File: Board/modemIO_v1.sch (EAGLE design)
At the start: 24 parts, among them IC1 TLV320AIC14R-PDSO-G30, IC2 SN74LVC04ADRR-PDSO-G14, Q1-18.432MHZ ASFL1

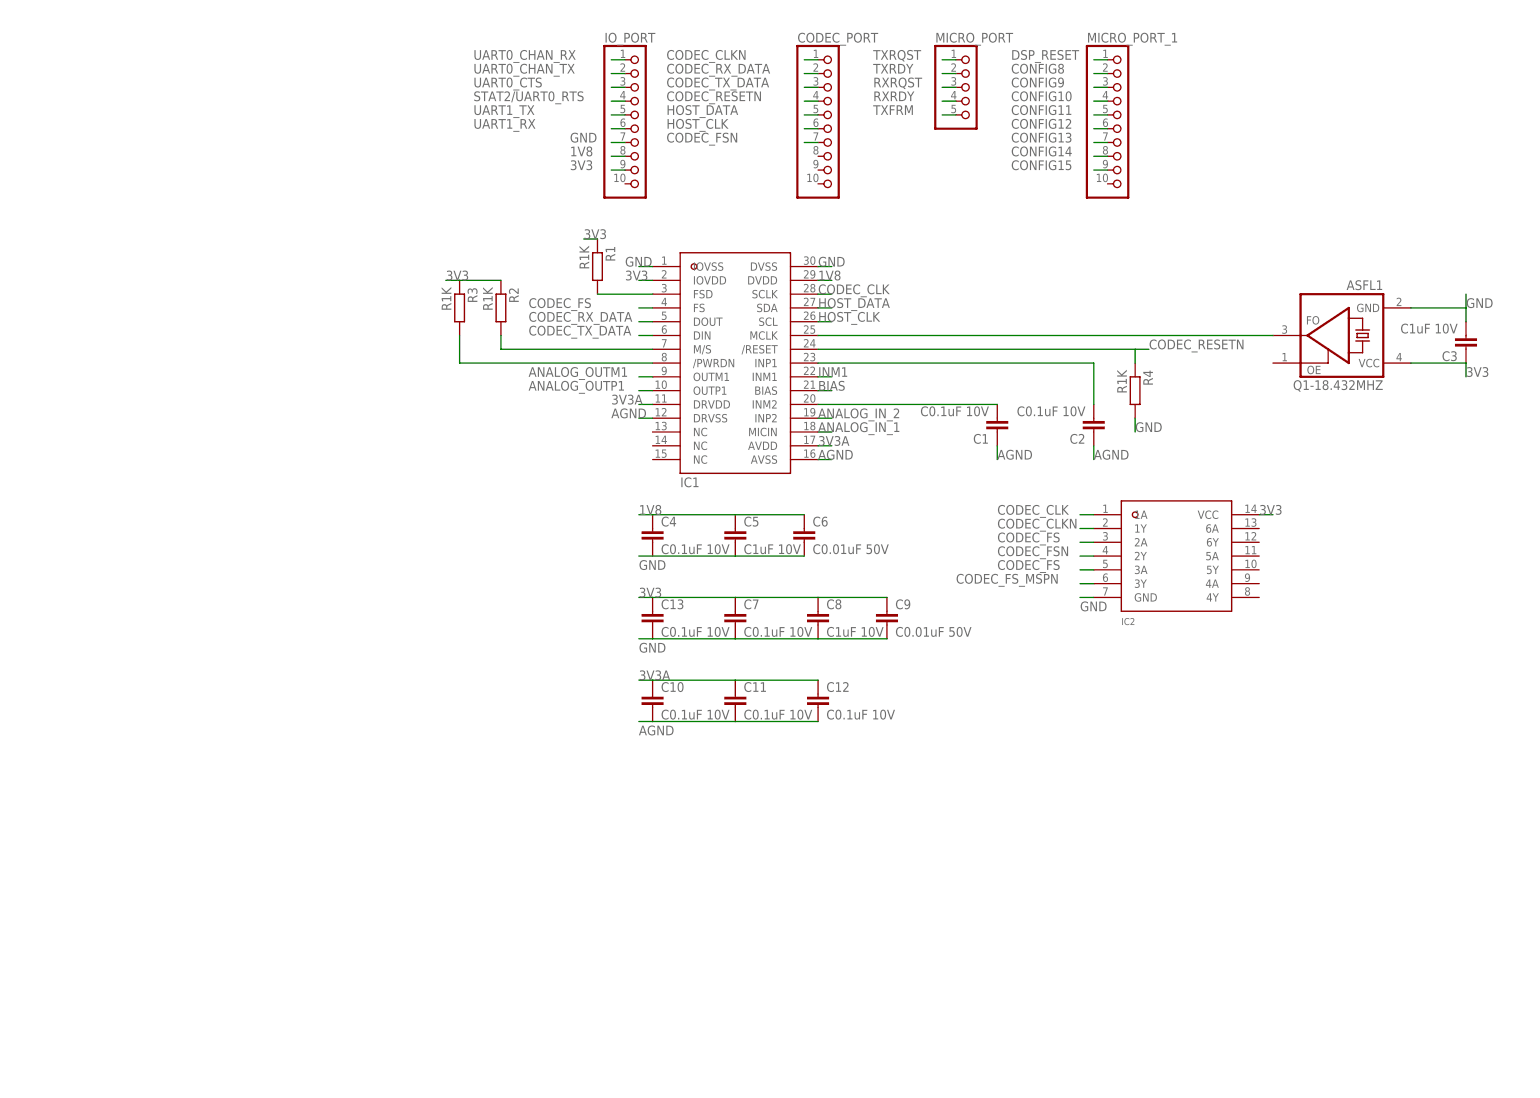
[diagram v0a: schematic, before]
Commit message: + pull up to AMBE's Reset & progress in ModemIO brd
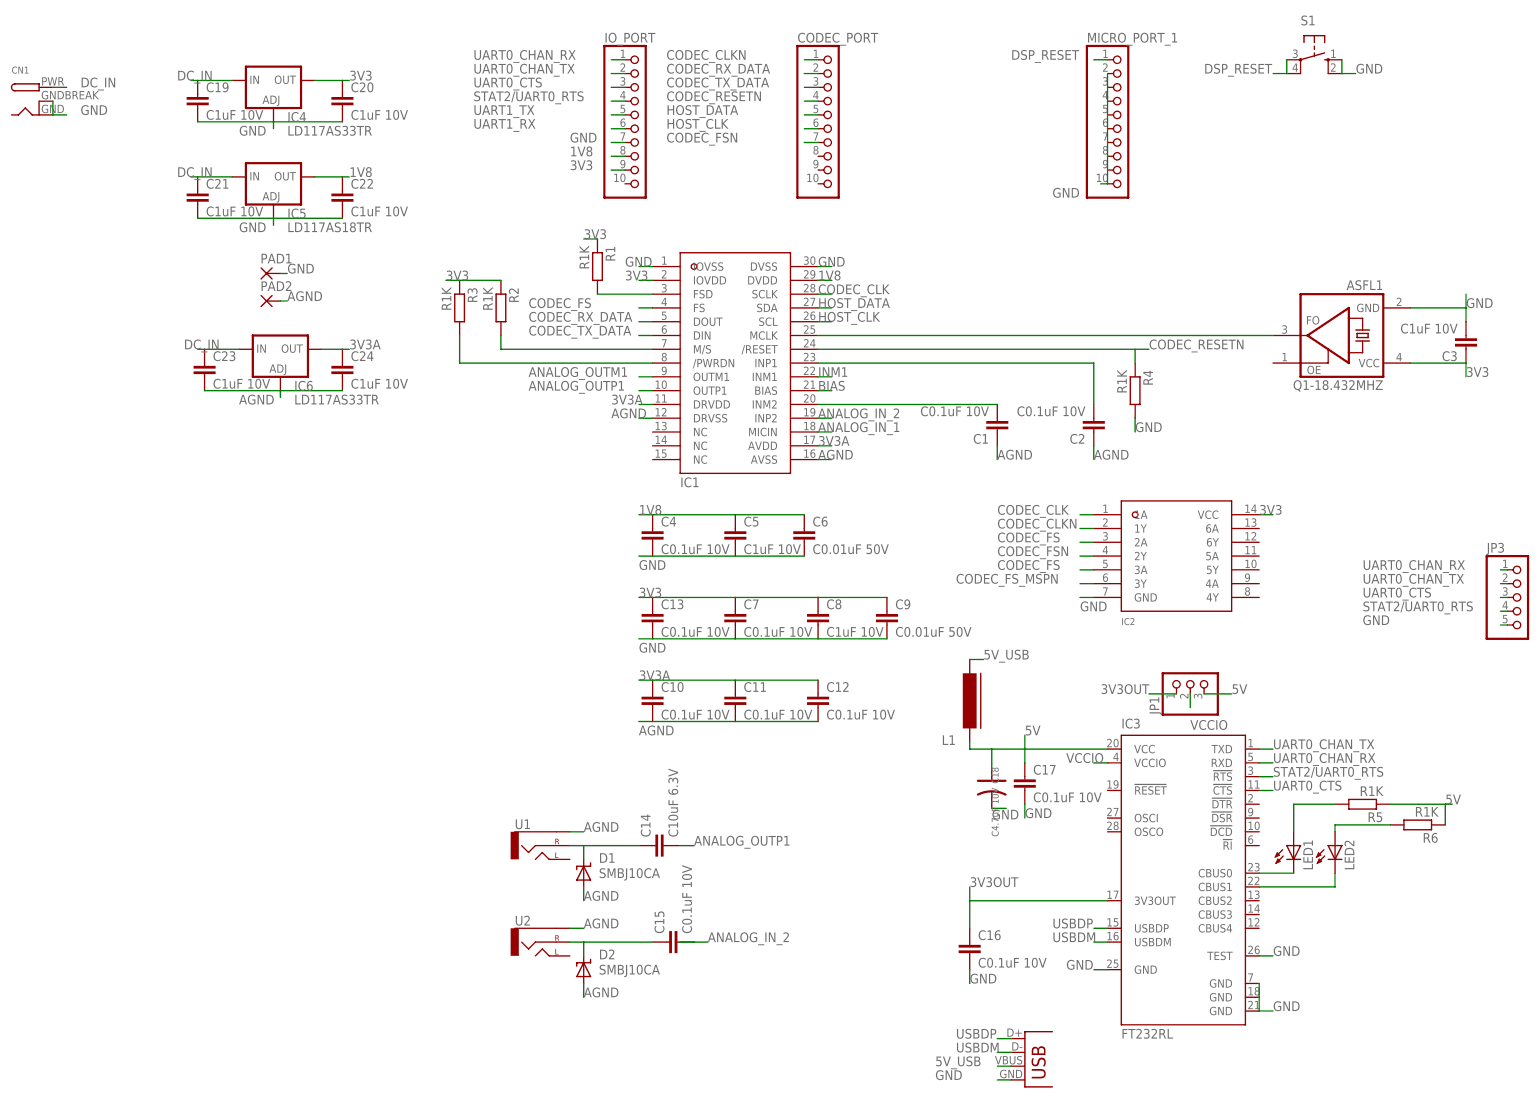
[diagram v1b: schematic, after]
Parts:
- removed MICRO_PORT: (no value), pinhead:PINHD-1X5
- added C14: C10uF 6.3V, resistor:C-EUC0805
- added C15, C16, C17: C0.1uF 10V, resistor:C-EUC0805
- added C18: C4.7uF 10V, OPL Eagle Library:C-POLAR-C
- added C19, C20, C21, C22, C23, C24: C1uF 10V, resistor:C-EUC0805
- added CN1: (no value), adafruit:DCBARRELPTH
- added D1, D2: SMBJ10CA, diode:SUPPRESSOR-SMBJ
- added IC3: FT232RL, ftdichip:FT232RL
- added IC4, IC6: LD117AS33TR, v-reg:LD117AS33TR
- added IC5: LD117AS18TR, v-reg:LD117AS18TR
- added JP1: (no value), pinhead:PINHD-1X3
- added JP2: USBSMD, SparkFun-Connectors:USBSMD
- added JP3: (no value), pinhead:PINHD-1X5
- added L1: (no value), dp_devices:FERRITE-0603
- added LED1, LED2: (no value), led:LEDCHIP-LED0805
- added PAD1, PAD2: (no value), wirepad:SMD2
- added R5, R6: R1K, resistor:R-EU_R0805
- added S1: (no value), switch-omron:10-XX
- added U1, U2: (no value), SparkFun-Connectors:AUDIO-JACKSMD2
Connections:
- removed net CONFIG10: MICRO_PORT_1.4
- removed net CONFIG11: MICRO_PORT_1.5
- removed net CONFIG12: MICRO_PORT_1.6
- removed net CONFIG13: MICRO_PORT_1.7
- removed net CONFIG14: MICRO_PORT_1.8
- removed net CONFIG15: MICRO_PORT_1.9
- removed net CONFIG8: MICRO_PORT_1.2
- removed net CONFIG9: MICRO_PORT_1.3
- removed net RXRDY: MICRO_PORT.4
- removed net RXRQST: MICRO_PORT.3
- removed net TXFRM: MICRO_PORT.5
- removed net TXRDY: MICRO_PORT.2
- removed net TXRQST: MICRO_PORT.1
- new net 3V3OUT: C16.1, IC3.3V3OUT, JP1.1
- new net 5V: C17.1, C18.1, IC3.VCC, JP1.3, L1.1, R5.1, R6.1
- new net 5V_USB: JP2.VBUS, L1.2
- new net DC_IN: C19.1, C21.1, C23.1, CN1.PWR, IC4.IN, IC5.IN, IC6.IN
- new net N$1: C14.1, D1.C, U1.RIGHT
- new net N$2: IC3.CBUS0, LED1.C
- new net N$4: IC3.CBUS1, LED2.C
- new net N$5: C15.1, D2.C, U2.RIGHT
- new net N$6: LED1.A, R5.2
- new net N$9: LED2.A, R6.2
- new net USBDM: IC3.USBDM, JP2.D-
- new net USBDP: IC3.USBDP, JP2.D+
- new net VCCIO: IC3.VCCIO, JP1.2
- net 1V8: now also C22.1, IC5.OUT
- net 3V3: now also C20.1, IC4.OUT
- net 3V3A: now also C24.1, IC6.OUT
- net AGND: now also C23.2, C24.2, D1.A, D2.A, IC6.ADJ, PAD2.P, U1.SLEEVE, U2.SLEEVE
- net ANALOG_IN_2: now also C15.2
- net ANALOG_OUTP1: now also C14.2
- net DSP_RESET: now also S1.P, S1.P1
- net GND: now also C16.2, C17.2, C18.2, C19.2, C20.2, C21.2, C22.2, C4.2, CN1.GND, CN1.GNDBREAK, IC3.GND, IC3.GND@1, IC3.GND@2, IC3.GND@A, IC3.TEST, IC4.ADJ, IC5.ADJ, JP2.GND, JP3.5, MICRO_PORT_1.10, MICRO_PORT_1.2, MICRO_PORT_1.3, MICRO_PORT_1.4, MICRO_PORT_1.5, MICRO_PORT_1.6, MICRO_PORT_1.7, MICRO_PORT_1.8, MICRO_PORT_1.9, PAD1.P, S1.S, S1.S1
- net STAT2/UART0_RTS: now also IC3.!RTS, JP3.4
- net UART0_CHAN_RX: now also IC3.RXD, JP3.1
- net UART0_CHAN_TX: now also IC3.TXD, JP3.2
- net UART0_CTS: now also IC3.!CTS, JP3.3
